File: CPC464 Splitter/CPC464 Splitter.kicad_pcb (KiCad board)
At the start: 2 copper layers, 81.9 x 40.6 mm, 21 parts, among them J1 Joystick 0, J2 Joystick 1, J3 CPC IDC, M1 Mounting, M2 Mounting, M3 Mounting, M4 Mounting, M5 Mounting, M6 Mounting

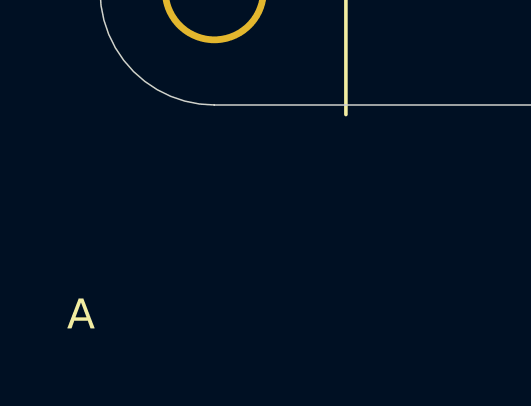
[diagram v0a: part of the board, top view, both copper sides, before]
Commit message: Added outline for faceplate
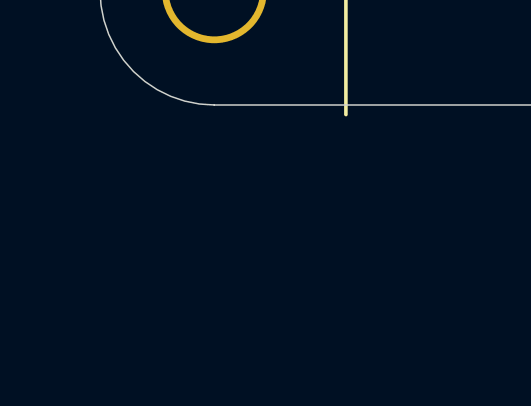
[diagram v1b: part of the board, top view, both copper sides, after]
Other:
- board text removed: "A"
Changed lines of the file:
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@@
   (general
     (thickness 1.6)
-    (drawings 22)
+    (drawings 51)
     (tracks 137)
     (zones 0)
@@
       (net 32 "Net-(M6-Pad1)") (solder_mask_margin 0.8))
   )
-  (gr_text A (at 98.425 119.38) (layer F.SilkS)
-    (effects (font (size 1 1) (thickness 0.15)))
-  )
+  (gr_arc (start 147.0025 108.839) (end 147.0025 109.474) (angle -90) (layer Dwgs.User) (width 0.05))
+  (gr_line (start 148.2725 100.2665) (end 165.0365 100.2665) (layer Dwgs.User) (width 0.05))
+  (gr_line (start 147.6375 100.9015) (end 147.6375 108.839) (layer Dwgs.User) (width 0.05))
+  (gr_line (start 141.1605 110.109) (end 141.1605 111.76) (layer Dwgs.User) (width 0.05))
+  (gr_arc (start 172.7835 111.76) (end 172.1485 111.76) (angle -90) (layer Dwgs.User) (width 0.05))
+  (gr_arc (start 140.5255 111.76) (end 140.5255 112.395) (angle -90) (layer Dwgs.User) (width 0.05))
+  (gr_arc (start 171.5135 110.109) (end 172.1485 110.109) (angle -90) (layer Dwgs.User) (width 0.05))
+  (gr_arc (start 141.7955 110.109) (end 141.7955 109.474) (angle -90) (layer Dwgs.User) (width 0.05))
+  (gr_arc (start 166.3065 108.839) (end 165.6715 108.839) (angle -90) (layer Dwgs.User) (width 0.05))
+  (gr_arc (start 148.2725 100.9015) (end 148.2725 100.2665) (angle -90) (layer Dwgs.User) (width 0.05))
+  (gr_line (start 165.6715 100.9015) (end 165.6715 108.839) (layer Dwgs.User) (width 0.05))
+  (gr_line (start 166.3065 109.474) (end 171.5135 109.474) (layer Dwgs.User) (width 0.05))
+  (gr_line (start 172.1485 110.109) (end 172.1485 111.76) (layer Dwgs.User) (width 0.05))
+  (gr_line (start 141.7955 109.474) (end 147.0025 109.474) (layer Dwgs.User) (width 0.05))
+  (gr_arc (start 165.0365 100.9015) (end 165.6715 100.9015) (angle -90) (layer Dwgs.User) (width 0.05))
+  (gr_arc (start 138.8745 111.76) (end 138.2395 111.76) (angle -90) (layer Dwgs.User) (width 0.05))
+  (gr_arc (start 106.6165 111.76) (end 106.6165 112.395) (angle -90) (layer Dwgs.User) (width 0.05))
+  (gr_line (start 138.2395 110.109) (end 138.2395 111.76) (layer Dwgs.User) (width 0.05))
+  (gr_arc (start 137.6045 110.109) (end 138.2395 110.109) (angle -90) (layer Dwgs.User) (width 0.05))
+  (gr_line (start 132.3975 109.474) (end 137.6045 109.474) (layer Dwgs.User) (width 0.05))
+  (gr_line (start 107.2515 110.109) (end 107.2515 111.76) (layer Dwgs.User) (width 0.05))
+  (gr_line (start 107.8865 109.474) (end 113.0935 109.474) (layer Dwgs.User) (width 0.05))
+  (gr_arc (start 107.8865 110.109) (end 107.8865 109.474) (angle -90) (layer Dwgs.User) (width 0.05))
+  (gr_arc (start 132.3975 108.839) (end 131.7625 108.839) (angle -90) (layer Dwgs.User) (width 0.05))
+  (gr_arc (start 113.0935 108.839) (end 113.0935 109.474) (angle -90) (layer Dwgs.User) (width 0.05))
+  (gr_arc (start 131.1275 100.9015) (end 131.7625 100.9015) (angle -90) (layer Dwgs.User) (width 0.05))
+  (gr_arc (start 114.3635 100.9015) (end 114.3635 100.2665) (angle -90) (layer Dwgs.User) (width 0.05))
+  (gr_line (start 131.7625 100.9015) (end 131.7625 108.839) (layer Dwgs.User) (width 0.05))
+  (gr_line (start 113.7285 100.9015) (end 113.7285 108.839) (layer Dwgs.User) (width 0.05))
+  (gr_line (start 114.3635 100.2665) (end 131.1275 100.2665) (layer Dwgs.User) (width 0.05))
   (gr_text "Revision A\ngithub.com/tebl" (at 177.165 92.075 90) (layer F.SilkS)
     (effects (font (size 1 1) (thickness 0.15)))
